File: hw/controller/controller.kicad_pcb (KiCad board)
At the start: 2 copper layers, 88.9 x 76.2 mm, 69 parts, among them P1 USB_OTG, P10 GPIO, P11 VDD_SEL, P12 UART0, P13 SPI, P14 I2C0, P15 I2C1, P16 I2C2, P17 I2C3, P18 I2C4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

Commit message: Passing DRC!
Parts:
- added SW1: RST, footprints:PTS645SM43SMTR92, F.Cu at (181.9, 88.6)
- added SW2: BOOT, footprints:PTS645SM43SMTR92, F.Cu at (181.9, 96.0)
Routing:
- net VDD: track 138.7 -> 303.6 mm, vias 0 -> 6
- net /VDD_ALT: track 44.0 -> 127.8 mm
- net +5V: track 47.7 -> 104.0 mm, vias 0 -> 2
- net /SCL7: track 0.00 -> 52.8 mm
- net /SDA7: track 0.00 -> 46.4 mm
- net /SCL6: track 0.00 -> 42.8 mm
- net /SCL4: track 0.00 -> 41.0 mm
- net /SCL5: track 0.00 -> 40.0 mm
- net /SDA0: track 6.37 -> 44.1 mm
- net /SDA6: track 0.00 -> 37.7 mm
- net /SDA4: track 0.00 -> 36.8 mm
- net GND: track 60.7 -> 96.9 mm, vias 7 -> 14
- net /SCL0: track 9.52 -> 45.1 mm
- net /SDA5: track 0.00 -> 33.8 mm
- net /SCL3: track 8.80 -> 39.5 mm
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- added copper zone on B.Cu, net GND
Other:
- board size 88.9 x 76.2 mm -> 82.5 x 76.2 mm

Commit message: Ostur Controller Layout 1.0 done!
I think...
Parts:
- added REF**: MountingHole_3mm, Mounting_Holes:MountingHole_3mm, F.Cu at (182.9, 102.9)
- added REF**: MountingHole_3mm, Mounting_Holes:MountingHole_3mm, F.Cu at (185.4, 147.3)
- added REF**: MountingHole_3mm, Mounting_Holes:MountingHole_3mm, F.Cu at (114.3, 134.6)
- added REF**: MountingHole_3mm, Mounting_Holes:MountingHole_3mm, F.Cu at (114.3, 94.0)
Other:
- board text added: "3 3 5 5"
- board text added: "3 A 5"
- board text added: "4B"
- board text added: "G G G G"
- board text added: "GPIO0-3"
- board text added: "GPIO3-7"
- board text added: "I2C0"
- board text added: "I2C1"
- board text added: "I2C2"
- board text added: "I2C3"
- board text added: "I2C4"
- board text added: "I2C5"
- board text added: "I2C6"
- board text added: "I2C7"
- board text added: "Ostur Controller v1.0"
- board text added: "SPI"
- board text added: "UART1"
- board text added: "UART3"
- board text added: "by @alvaroprieto"
- board text added: "dfu"
- board text added: "fan"
- board text added: "fridge"
- board text added: "mist"
- board text added: "pump"
- board text added: "rst"
- board text added: "swd"

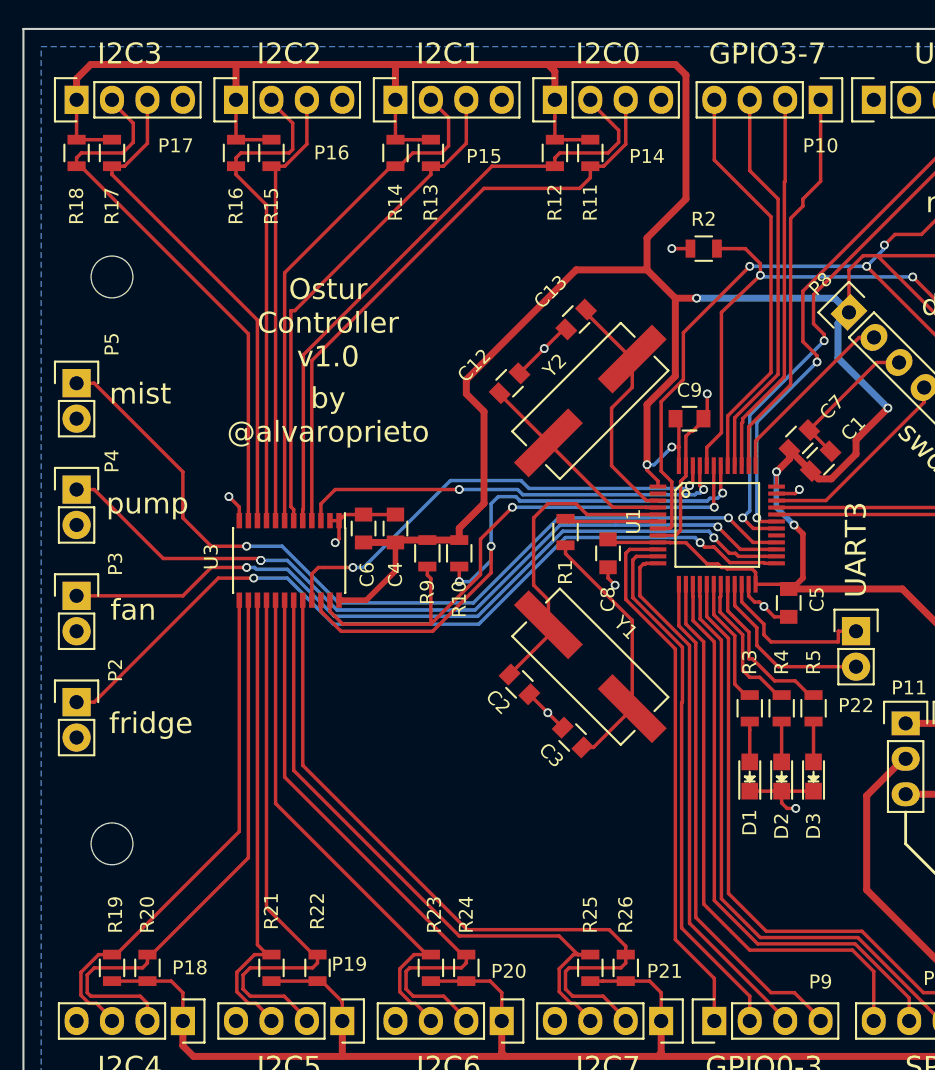
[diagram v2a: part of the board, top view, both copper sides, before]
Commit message: Fixed GPIO label and moved resistor
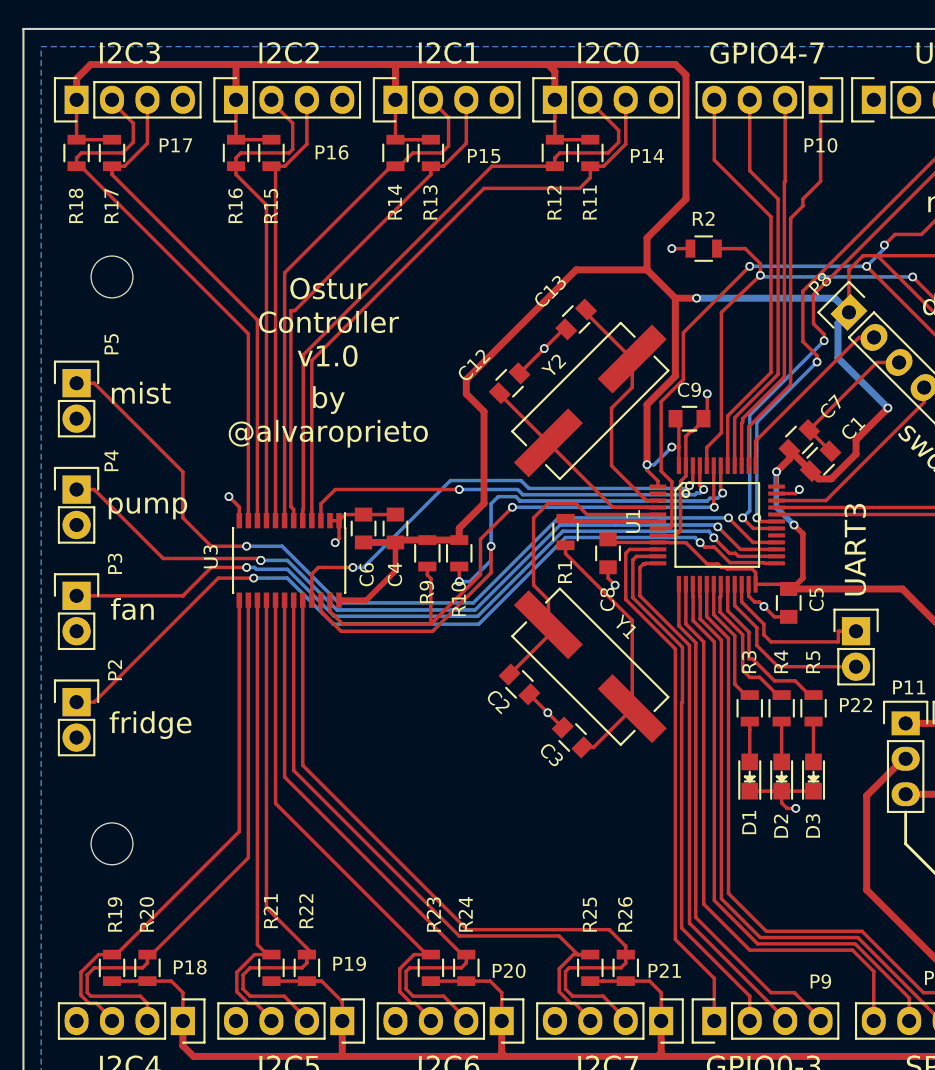
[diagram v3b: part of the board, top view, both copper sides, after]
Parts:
- moved R22 0.76 mm to (128.3, 143.5)
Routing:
- net /SCL5: track 40.0 -> 39.0 mm
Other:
- board text added: "GPIO4-7"
- board text removed: "GPIO3-7"
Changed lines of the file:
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@@
     (thickness 1.6)
     (drawings 41)
-    (tracks 831)
+    (tracks 830)
     (zones 0)
     (modules 75)
@@
   )
   (setup
-    (last_trace_width 0.4)
+    (last_trace_width 0.25)
     (user_trace_width 0.25)
     (user_trace_width 0.4)
@@
   )
   (module Resistors_SMD:R_0805 (layer F.Cu)
-    (at 129.032 143.51 90)
+    (at 128.27 143.51 90)
     (descr "Resistor SMD 0805, reflow soldering, Vishay (see dcrcw.pdf)")
     (tags "resistor 0805")
@@
     (effects (font (size 1.5 1.5) (thickness 0.3)))
   )
-  (gr_text GPIO3-7 (at 161.29 77.978) (layer F.SilkS)
+  (gr_text GPIO4-7 (at 161.29 77.978) (layer F.SilkS)
     (effects (font (size 1.5 1.5) (thickness 0.3)))
   )
@@
     (effects (font (size 1.5 1.5) (thickness 0.3)))
   )
-  (gr_text I2C3 (at 115.57 77.978 360) (layer F.SilkS)
+  (gr_text I2C3 (at 115.57 77.978) (layer F.SilkS)
     (effects (font (size 1.5 1.5) (thickness 0.3)))
   )
-  (gr_text I2C2 (at 127 77.978 360) (layer F.SilkS)
+  (gr_text I2C2 (at 127 77.978) (layer F.SilkS)
     (effects (font (size 1.5 1.5) (thickness 0.3)))
   )
-  (gr_text I2C0 (at 149.86 77.978 360) (layer F.SilkS)
+  (gr_text I2C0 (at 149.86 77.978) (layer F.SilkS)
     (effects (font (size 1.5 1.5) (thickness 0.3)))
   )
-  (gr_text I2C1 (at 138.43 77.978 360) (layer F.SilkS)
+  (gr_text I2C1 (at 138.43 77.978) (layer F.SilkS)
     (effects (font (size 1.5 1.5) (thickness 0.3)))
   )
@@
   (segment (start 114.6 142.56) (end 114.3 142.56) (width 0.25) (layer F.Cu) (net 47))
   (segment (start 123.425 133.735) (end 114.6 142.56) (width 0.25) (layer F.Cu) (net 47))
-  (segment (start 129.032 142.56) (end 129.032 143.16) (width 0.25) (layer F.Cu) (net 48))
-  (segment (start 129.032 143.16) (end 128.682 143.51) (width 0.25) (layer F.Cu) (net 48))
-  (segment (start 128.682 143.51) (end 124.206 143.51) (width 0.25) (layer F.Cu) (net 48))
+  (segment (start 127.92 143.51) (end 124.206 143.51) (width 0.25) (layer F.Cu) (net 48))
+  (segment (start 128.27 142.56) (end 128.27 143.16) (width 0.25) (layer F.Cu) (net 48))
+  (segment (start 128.27 143.16) (end 127.92 143.51) (width 0.25) (layer F.Cu) (net 48))
   (segment (start 124.206 143.51) (end 123.698 144.018) (width 0.25) (layer F.Cu) (net 48))
   (segment (start 123.698 144.018) (end 123.698 145.034) (width 0.25) (layer F.Cu) (net 48))
@@
   (segment (start 125.375 117.15) (end 125.375 139.203) (width 0.25) (layer F.Cu) (net 48))
   (segment (start 125.375 139.203) (end 128.732 142.56) (width 0.25) (layer F.Cu) (net 48))
-  (segment (start 128.732 142.56) (end 129.032 142.56) (width 0.25) (layer F.Cu) (net 48))
   (segment (start 125.73 142.56) (end 124.51959 142.56) (width 0.25) (layer F.Cu) (net 49))
   (segment (start 124.51959 142.56) (end 123.24799 143.8316) (width 0.25) (layer F.Cu) (net 49))

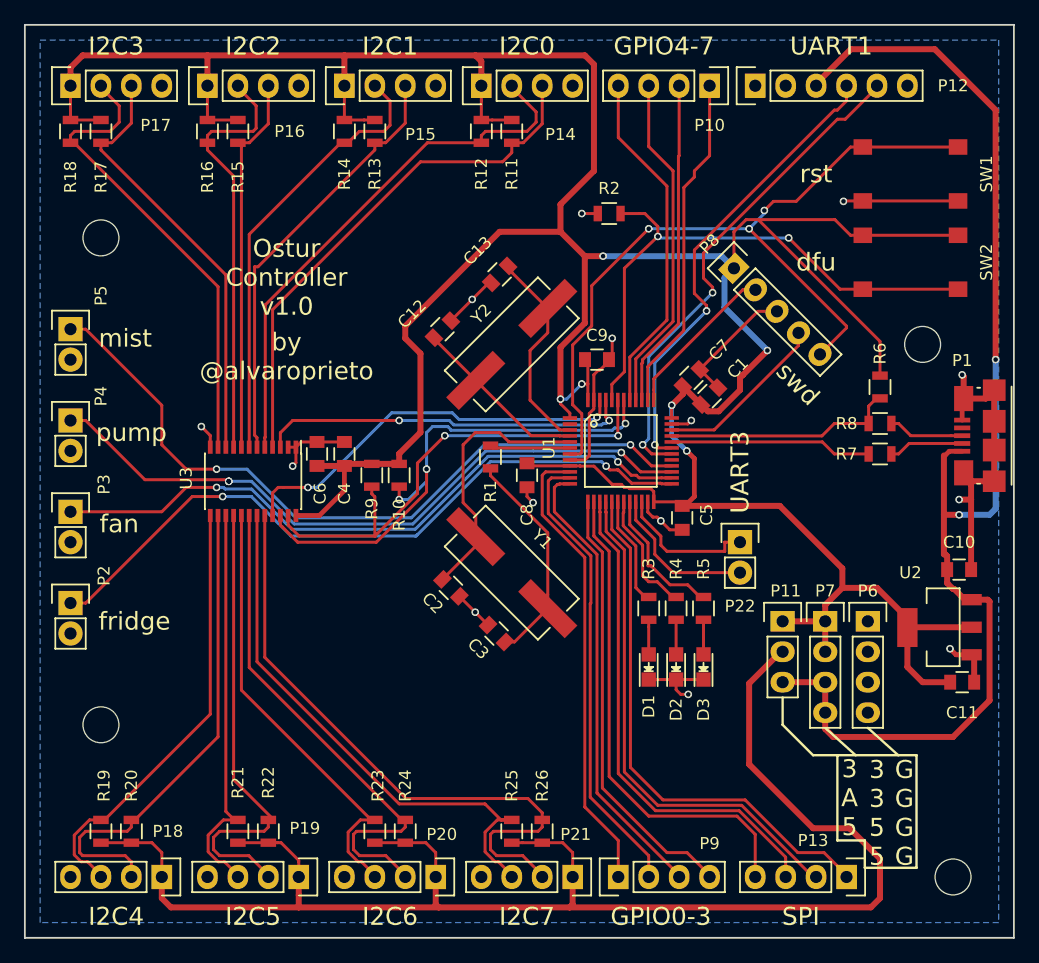
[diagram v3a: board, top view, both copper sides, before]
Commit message: Updated ostur controller to v1.1
Some changes:
Reduced i2c to 4 channels instead of 8
Added ARM-SWD 10-pin connector
Removed 8MHz crystal (not needed for usb)
Added actual footprint for 32.768kHz crystal
Moved uart, not sure why though...
Smaller board!
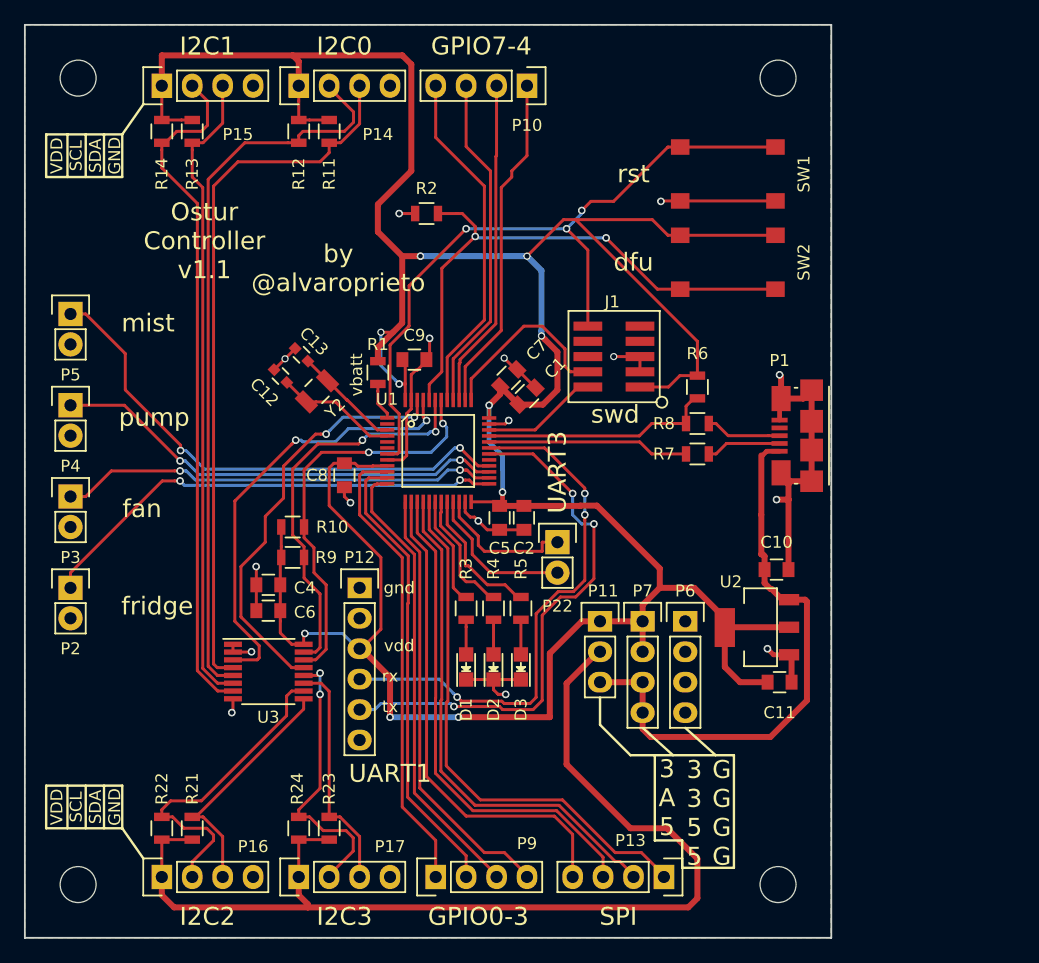
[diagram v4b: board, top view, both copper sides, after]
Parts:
- removed C3: 20pF, Capacitors_SMD:C_0805
- removed P18: I2C4, Pin_Headers:Pin_Header_Straight_1x04
- removed P19: I2C5, Pin_Headers:Pin_Header_Straight_1x04
- removed P20: I2C6, Pin_Headers:Pin_Header_Straight_1x04
- removed P21: I2C7, Pin_Headers:Pin_Header_Straight_1x04
- removed P8: SWD, Pin_Headers:Pin_Header_Straight_1x05
- removed R15, R16, R17, R18, R19, R20, R25, R26: 10k, Resistors_SMD:R_0805
- removed Y1: 8MHz, footprints:ATS-SM-CRYSTAL
- added J1: ARM-SWD, footprints:ARM_SWD_SMD, F.Cu at (157.1, 103.9)
- C1: value 10nF -> 100nF
- C11: value 10nF -> 10uF
- C12, C13: value 22pF -> 12pF; footprint Capacitors_SMD:C_0805 -> Capacitors_SMD:C_0603
- C2: value 20pF -> 10nF
- C7, C9: value 100nF -> 4.7uF
- C8: value 100nF -> 1uF
- R1: value 390 -> 0
- U3: value tca9548a -> tca9546a; footprint Housings_SSOP:TSSOP-24_4.4x7.8mm_Pitch0.65mm -> Housings_SSOP:TSSOP-16_4.4x5mm_Pitch0.65mm
- Y2: footprint footprints:ATS-SM-CRYSTAL -> footprints:FC-135
- moved P17 68.7 mm to (130.8, 147.3)
- moved P16 66.1 mm to (119.4, 147.3)
- moved P12 53.4 mm to (135.9, 123.2), turned to 0 degrees
- moved REF** 25.3 mm to (170.8, 80.6)
- moved C13 17.8 mm to (131.0, 103.7), turned to 135 degrees
- moved Y2 16.7 mm to (132.3, 106.8), turned to 225 degrees
- moved U3 15.9 mm to (128.3, 130.2), turned to 0 degrees
- moved C10 15.2 mm to (170.7, 121.7)
- moved C8 15.2 mm to (134.6, 113.8)
- moved C9 15.2 mm to (140.5, 104.1)
- moved D1 15.2 mm to (144.8, 129.8)
- moved D2 15.2 mm to (147.1, 129.8)
- moved D3 15.2 mm to (149.4, 129.8)
- moved P11 15.2 mm to (156.0, 126.0)
- moved P13 15.2 mm to (161.3, 147.3)
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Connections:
- C2 pad 1: Net-(C2-Pad1) -> VDD
- P12 pad 3: +5V -> VDD
- P16 pad 1: VDD -> /VDD_ALT
- P17 pad 1: VDD -> /VDD_ALT
- R1 pad 1: Net-(R1-Pad1) -> VDD
- R1 pad 2: Net-(C3-Pad1) -> Net-(R1-Pad2)
- R21 pad 2: /SDA5 -> /SDA2
- R22 pad 2: /SCL5 -> /SCL2
- R23 pad 2: /SDA6 -> /SDA3
- R24 pad 2: /SCL6 -> /SCL3
- U1 pad 1: VDD -> Net-(R1-Pad2)
- U1 pad 5: Net-(C2-Pad1) -> Net-(U1-Pad5)
- U1 pad 6: Net-(R1-Pad1) -> Net-(U1-Pad6)
- U3 pad 10: /SDA3 -> /SCL2
- U3 pad 11: /SCL3 -> /SDA3
- U3 pad 12: GND -> /SCL3
- U3 pad 13: /SDA4 -> /TCA_A2
- U3 pad 14: /SCL4 -> /SCL
- U3 pad 15: /SDA5 -> /SDA
- U3 pad 16: /SCL5 -> VDD
- U3 pad 8: /SDA2 -> GND
- U3 pad 9: /SCL2 -> /SDA2
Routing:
- net +5V: track 104.0 -> 47.7 mm, vias 2 -> 0
- net /SCL7: track 52.8 -> 0.00 mm
- net /SDA7: track 46.4 -> 0.00 mm
- net /SCL6: track 42.8 -> 0.00 mm
- net /SCL4: track 41.0 -> 0.00 mm
- net /SCL5: track 39.0 -> 0.00 mm
- net /VDD_ALT: track 127.8 -> 89.3 mm
- net /SDA6: track 37.7 -> 0.00 mm
- net /SDA4: track 36.8 -> 0.00 mm
- net /SDA5: track 33.8 -> 0.00 mm
- net Net-(C2-Pad1): track 22.5 -> 0.00 mm
- net VDD: track 303.6 -> 282.2 mm, vias 6 -> 10
- net /SCL1: track 37.1 -> 57.5 mm
- net /FAN: track 55.9 -> 36.8 mm
- net /PUMP: track 57.0 -> 38.2 mm, vias 3 -> 2
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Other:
- board size 82.5 x 76.2 mm -> 67.3 x 76.2 mm
- board text added: "GPIO7-4"
- board text added: "Ostur Controller v1.1"
- board text added: "VDD SCL SDA GND"
- board text added: "gnd"
- board text added: "rx"
- board text added: "tx"
- board text added: "vbatt"
- board text added: "vdd"
- board text removed: "GPIO4-7"
- board text removed: "I2C4"
- board text removed: "I2C5"
- board text removed: "I2C6"
- board text removed: "I2C7"
- board text removed: "Ostur Controller v1.0"
